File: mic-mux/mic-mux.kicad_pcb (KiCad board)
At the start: 4 copper layers, 142.2 x 203.2 mm, 325 parts, among them J1 MIC-IN, J10 I2C and Reset (Top-Male), J11 Power Out (Top-Male), J12 Extra GPIO, J2 MIC-OUT, J3 Headphone MUX Audio IN (Top-M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, J4 Headphone MUX Audio OUT (Top-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, J5 I2C and Reset, J6 Power In, J7 Headphone MUX Audio IN (Botto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, J8 Headphone MUX Audio OUT (Bott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, J9 GND, U1 ADG715, U10 TCA9555, U11 TCA9555, U12 OPA1604, U13 DS1882, U14 OPA1604, U15 DS1882, U16 OPA1604, U17 DS1882, U18 OPA1604, U19 DS1882, U2 ADG708, U20 OPA1604, U21 OPA1602, U22 OPA1604, U23 OPA1604, U24 OPA1604, U25 OPA1604, U26 OPA1602, U27 OPA1604, U28 OPA1604, U29 OPA1604, U3 ADG708, U30 OPA1604, U31 OPA1602, U32 OPA1604, U33 OPA1604, U34 OPA1604, U35 OPA1604, U36 OPA1602, U37 OPA1604, U38 OPA1604, U39 OPA1604, U4 ADG708, U5 ADG708, U6 ADG708, U7 ADG708, U8 ADG708, U9 ADG708

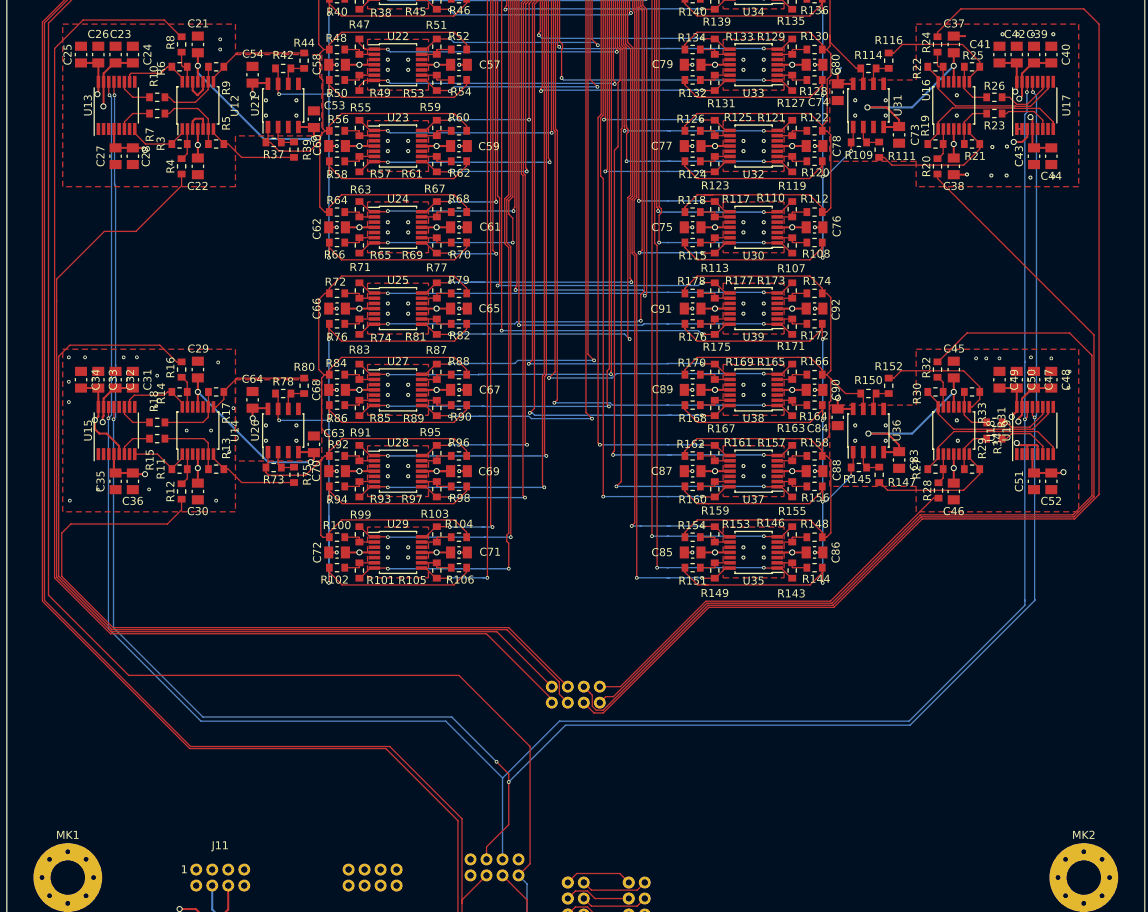
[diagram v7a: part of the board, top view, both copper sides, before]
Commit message: Moved mic mux audio in connector for motherboard layout porposies
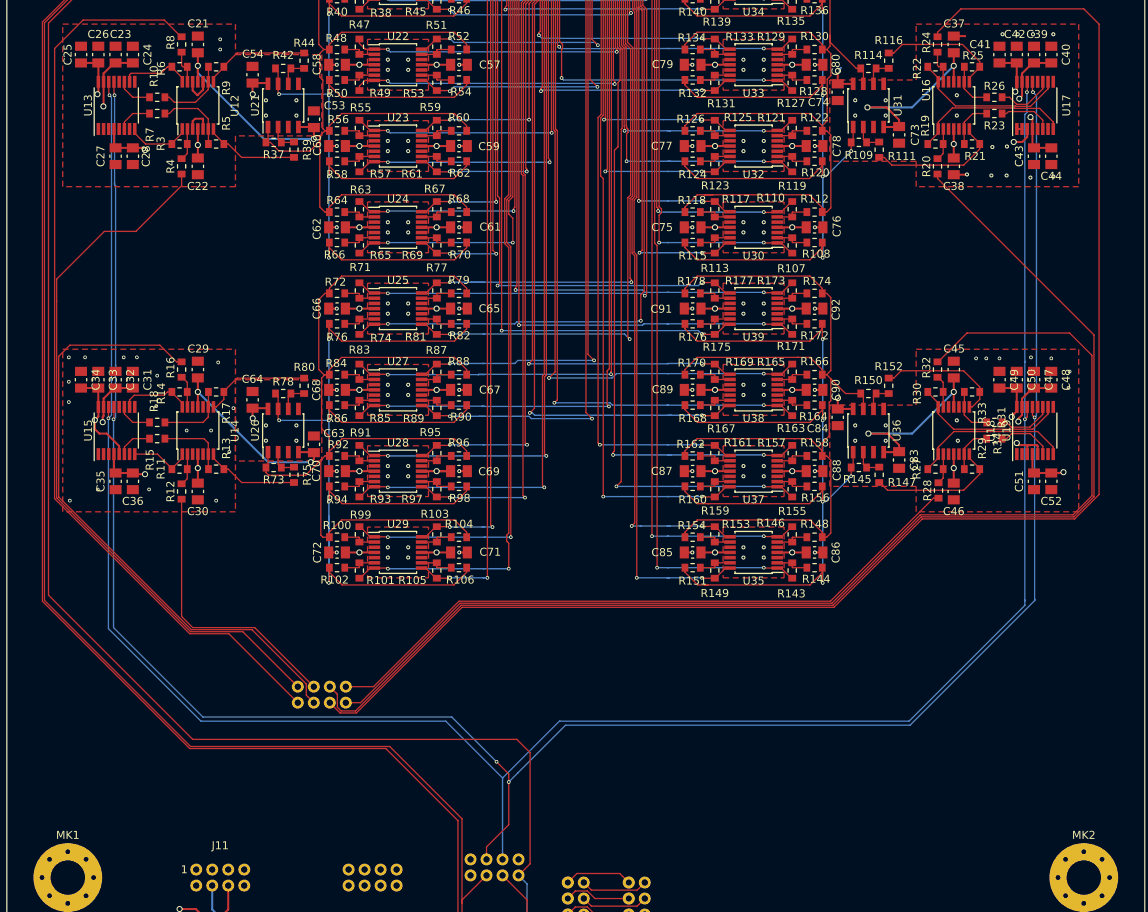
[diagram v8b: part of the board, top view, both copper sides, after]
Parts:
- moved J1 31.8 mm to (95.2, 269.2)
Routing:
- net /MIC-IN2: track 91.9 -> 34.8 mm
- net /MIC-IN1: track 153.3 -> 115.4 mm
- net /MIC-IN3: track 115.4 -> 77.7 mm
- net /MIC-IN0: track 126.8 -> 89.3 mm
- net /MIC-IN4: track 125.3 -> 157.3 mm
- net /MIC-IN7: track 111.7 -> 143.5 mm
- net /MIC-IN6: track 52.1 -> 83.8 mm
- net /MIC-IN5: track 157.8 -> 189.5 mm
- net +5V: track 410.0 -> 394.8 mm
- net +5VA: track 360.7 -> 346.6 mm
- net -5VA: track 333.3 -> 320.3 mm
